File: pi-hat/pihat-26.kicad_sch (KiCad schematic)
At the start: 11 parts, among them J1 Raspberry_Pi_4, J10 Conn_01x02_Pin, J11 Conn_01x02_Pin, J12 Conn_01x02_Pin, J2 Conn_01x10_Pin, J3 Conn_01x02_Pin, J4 Conn_01x02_Pin, J5 Conn_01x02_Pin, J6 Conn_01x02_Pin, J7 Conn_01x02_Pin, J9 Conn_01x02_Pin

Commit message: Update 40 Pin Connector to KiCad template one
Also added reset button, and removed the connection to pins 27/28 which
are used for flashing the Rasperry PI config through an EEPROM, which we
don't need to do.
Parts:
- removed J1: Raspberry_Pi_4, symbol Connector:Raspberry_Pi_4
- removed J2: Conn_01x10_Pin, Package_DFN_QFN:QFN-20-1EP_5x5mm_P0.65mm_EP3.35x3.35mm, symbol Connector:Conn_01x10_Pin
- removed J9: Conn_01x02_Pin, Connector_Molex:Molex_Mini-Fit_Jr_5566-02A_2x01_P4.20mm_Vertical, symbol Connector:Conn_01x02_Pin
- added J8: GPIO, Connector_PinSocket_2.54mm:PinSocket_2x20_P2.54mm_Vertical, symbol Connector_Generic:Conn_02x20_Odd_Even
- added SW1: SW_Push, Button_Switch_THT:SW_NKK_GW12LJP, symbol Switch:SW_Push
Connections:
- net GND: now also J8.14 (Pin_14), J8.20 (Pin_20), J8.25 (Pin_25), J8.30 (Pin_30), J8.34 (Pin_34), J8.39 (Pin_39), J8.6 (Pin_6), J8.9 (Pin_9), SW1.2
- net GPIO24: now also J8.18 (Pin_18)
- net GPIO25: now also J8.22 (Pin_22)
- net GPIO26: now also J8.37 (Pin_37)
- net GPIO27: now also J8.13 (Pin_13)
- net 3_SCL_UART-RX renamed GPIO5/RXD3/SCL3
- net GPIO5/RXD3/SCL3: now also J8.29 (Pin_29)
- net 3_SDA_UART-TX renamed GPIO4/TXD3/SDA3
- net GPIO4/TXD3/SDA3: now also J8.7 (Pin_7)
- net SCL1 renamed GPIO3/SCL1
- net GPIO3/SCL1: now also J8.5 (Pin_5)
- net SCL4 renamed GPIO7/SCL4
- net GPIO7/SCL4: now also J8.26 (Pin_26)
- net SCL5 renamed GPIO11/SCL5
- net GPIO11/SCL5: now also J8.23 (Pin_23)
- net SCL6 renamed GPIO23/SCL6
- net GPIO23/SCL6: now also J8.16 (Pin_16)
- net SDA1 renamed GPIO2/SDA1
- net GPIO2/SDA1: now also J8.3 (Pin_3)
- net SDA4 renamed GPIO6/SDA4
- net GPIO6/SDA4: now also J8.31 (Pin_31)
- net SDA5 renamed GPIO10/SDA5
- net GPIO10/SDA5: now also J8.19 (Pin_19)
- net SDA6 renamed GPIO22/SDA6
- net GPIO22/SDA6: now also J8.15 (Pin_15)
- net UART0-RX renamed GPIO15/RXD0
- net GPIO15/RXD0: now also J8.10 (Pin_10)
- net UART0-TX renamed GPIO14/TXD0
- net GPIO14/TXD0: now also J8.8 (Pin_8)
- net UART4-RX renamed GPIO9/RXD4
- net GPIO9/RXD4: now also J8.21 (Pin_21)
- net UART4-TX renamed GPIO8/TXD4
- net GPIO8/TXD4: now also J8.24 (Pin_24)
- net UART5-RX renamed GPIO13/RXD5
- net GPIO13/RXD5: now also J8.33 (Pin_33)
- net UART5-TX renamed GPIO12/TXD5
- net GPIO12/TXD5: now also J8.32 (Pin_32)
- new net +3V3: J8.1 (Pin_1), J8.17 (Pin_17)
- new net +5V: J8.2 (Pin_2), J8.4 (Pin_4)
- new net GPIO16: J8.36 (Pin_36)
- new net GPIO17: J8.11 (Pin_11), SW1.1
- new net GPIO18/PCM.CLK: J8.12 (Pin_12)
- new net GPIO19/PCM.FS: J8.35 (Pin_35)
- new net GPIO20/PCM.DIN: J8.38 (Pin_38)
- new net GPIO21/PCM.DOUT: J8.40 (Pin_40)
- no-connect marks 0 -> 2
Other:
- note added: "Extended throughhole for exposing pins on the HAT. And connction to the PI"
- note added: "PIN: 27/28 is for EEPROM flashing"
- note added: "Programmable Button for Rebooting or Relaunching UI"
- note added: "Setting GPIO Alternate Functions https://www.raspberrypi.com/documentation/computers/config_txt.html#gpio-control"
- note added: "TODO: Test all UART and I2C pins, to prove they actually work, because data sheet says they do but I don't believe it Reset Button, Reboots the PI, Reboots UI? Status LEDs?"
- note removed: "GPIO 10 - SDA5 GPIO 11 - SCL5"
- note removed: "GPIO 12 - UART5_TX GPIO 13 - UART5_RX"
- note removed: "GPIO 14 - UART0-TX GPIO 15 - UART0-RX"
- note removed: "GPIO 2 - SDA1 GPIO 3 - SCL1"
- note removed: "GPIO 22 - SDA6 GPIO 23 - SCL6"
- note removed: "GPIO 8 - UART4_TX GPIO 9 - UART4_RX"
- note removed: "GPIO0 - SDA0 || UART2-TX GPIO1 - SCL0 || UART2-RX"
- note removed: "GPIO4 - SDA3 || UART3-TX GPIO5 - SCL3 || UART3-RX"
- note removed: "GPIO6 - SDA4 GPIO7 - SCL4"
- moved on the sheet: J10, J11, J12, J3, J4, J5, J6, J7

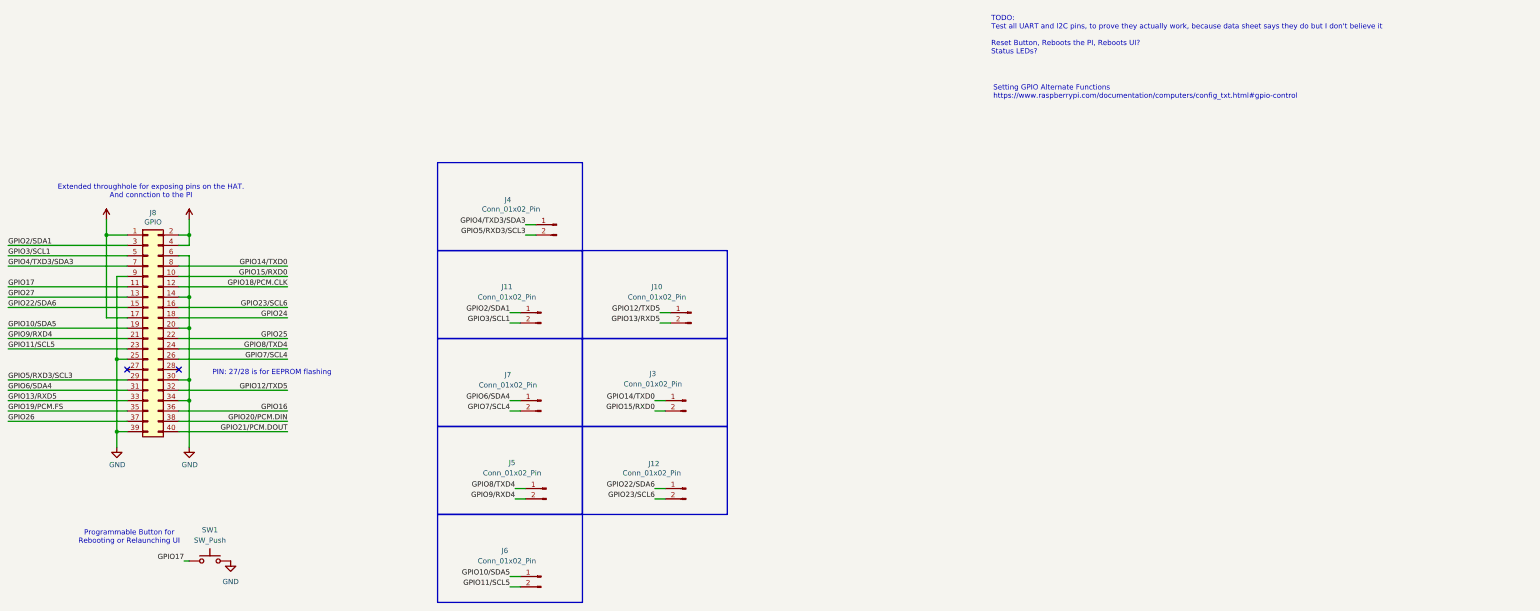
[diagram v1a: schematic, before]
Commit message: Reorganize and add 2 status LEDs to schematic
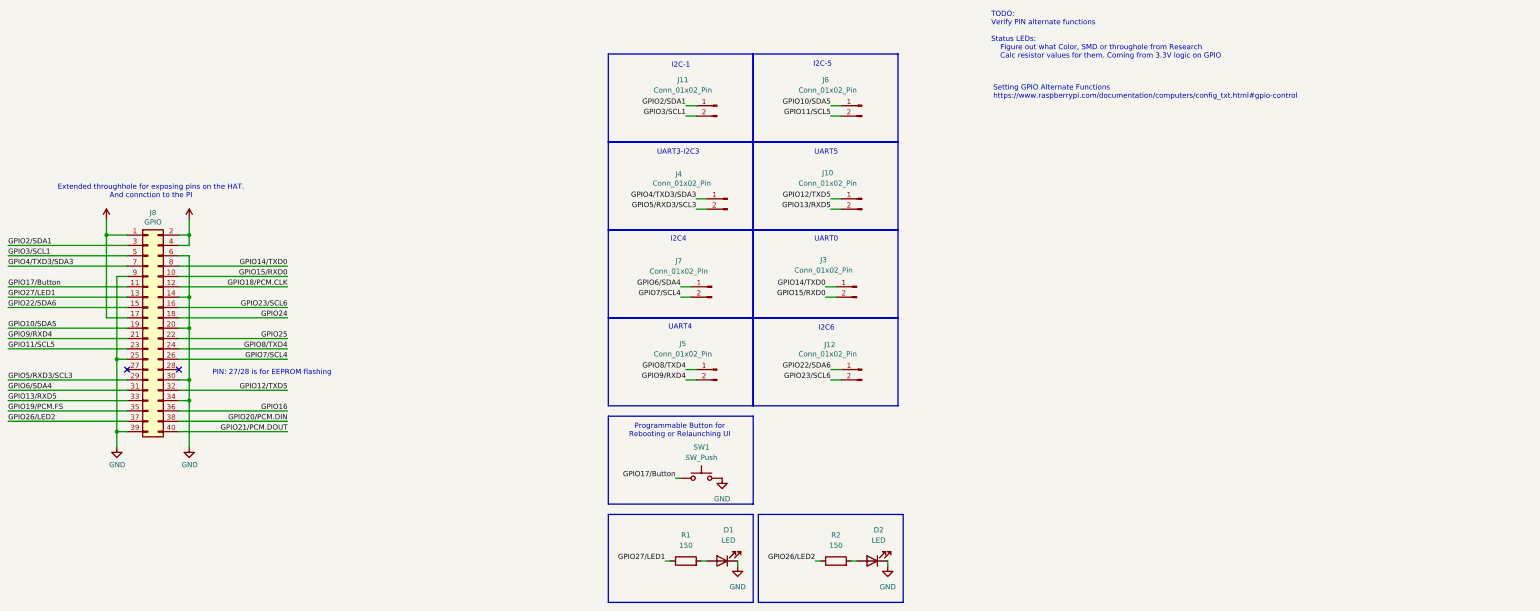
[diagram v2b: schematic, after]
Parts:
- added D1, D2: LED, symbol Device:LED
- added R1, R2: 150, symbol Device:R
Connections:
- net GND: now also D1.1 (K), D2.1 (K)
- net GPIO17 renamed GPIO17/Button
- net GPIO26 renamed GPIO26/LED2
- net GPIO26/LED2: now also R2.1
- net GPIO27 renamed GPIO27/LED1
- net GPIO27/LED1: now also R1.1
- new net: D2.2 (A), R2.2
- new net: D1.2 (A), R1.2
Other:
- note added: "I2C-1"
- note added: "I2C-5"
- note added: "I2C4"
- note added: "I2C6"
- note added: "TODO: Verify PIN alternate functions Status LEDs: Figure out what Color, SMD or throughole from Research Calc resistor values for them. Coming from 3.3V logic on GPIO"
- note added: "UART0"
- note added: "UART3-I2C3"
- note added: "UART4"
- note added: "UART5"
- note removed: "TODO: Test all UART and I2C pins, to prove they actually work, because data sheet says they do but I don't believe it Reset Button, Reboots the PI, Reboots UI? Status LEDs?"
- moved on the sheet: J10, J11, J12, J3, J4, J5, J6, J7, SW1

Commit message: Add Green,Red LED resistor values
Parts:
- R2: value 150 -> 120
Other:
- note added: "(3.3-2.2)/10mA = ~120"
- note added: "(3.3-2V)/10mA = ~150"
- note added: "GREEN-LED, 2.2V"
- note added: "RED-LED, 2V"
- note added: "TODO: Get actual LED specs if these aren't good enough"
- note added: "TODO: Verify PIN alternate functions"
- note removed: "TODO: Verify PIN alternate functions Status LEDs: Figure out what Color, SMD or throughole from Research Calc resistor values for them. Coming from 3.3V logic on GPIO"
- moved on the sheet: D1, D2, J10, J11, J12, J3, J4, J5, J6, J7, J8, R1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

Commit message: Add footprints to LED and Resistors
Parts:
- D1, D2: footprint (none) -> LED_SMD:LED_0805_2012Metric_Pad1.15x1.40mm_HandSolder
- R1, R2: footprint (none) -> Resistor_SMD:R_1206_3216Metric_Pad1.30x1.75mm_HandSolder
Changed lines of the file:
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@@
 			)
 		)
-		(property "Footprint" ""
+		(property "Footprint" "Resistor_SMD:R_1206_3216Metric_Pad1.30x1.75mm_HandSolder"
 			(at 106.68 164.338 90)
 			(hide yes)
@@
 			)
 		)
-		(property "Footprint" ""
+		(property "Footprint" "LED_SMD:LED_0805_2012Metric_Pad1.15x1.40mm_HandSolder"
 			(at 80.01 162.56 0)
 			(hide yes)
@@
 			)
 		)
-		(property "Footprint" ""
+		(property "Footprint" "LED_SMD:LED_0805_2012Metric_Pad1.15x1.40mm_HandSolder"
 			(at 115.57 162.56 0)
 			(hide yes)
@@
 			)
 		)
-		(property "Footprint" ""
+		(property "Footprint" "Resistor_SMD:R_1206_3216Metric_Pad1.30x1.75mm_HandSolder"
 			(at 71.12 164.338 90)
 			(hide yes)

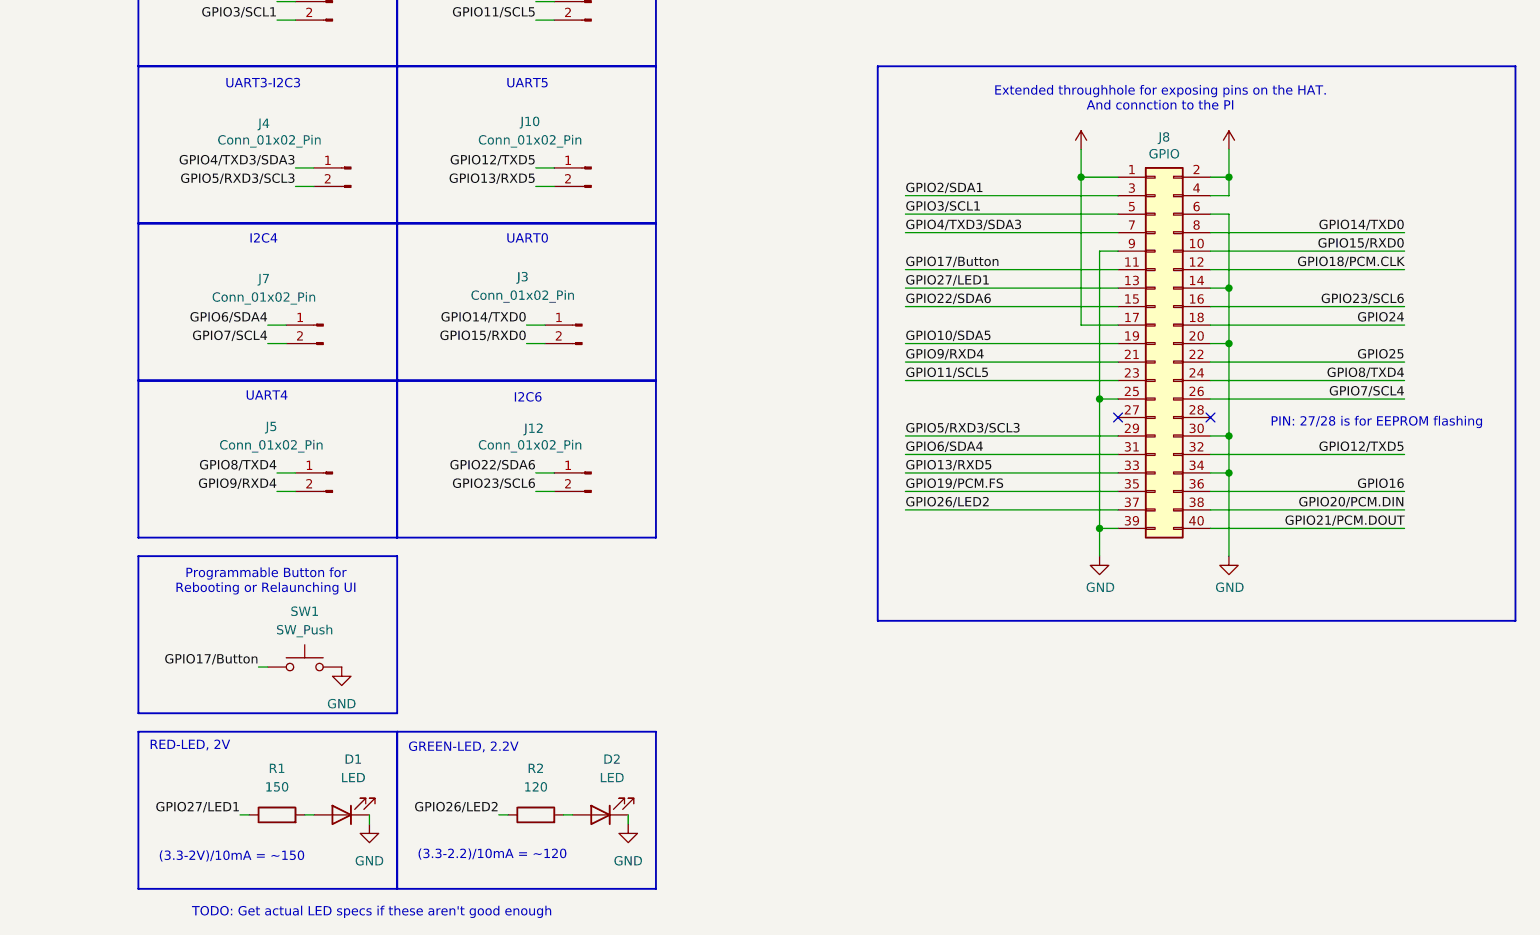
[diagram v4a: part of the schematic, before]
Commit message: Fix ERC errors
my goat swizz ty
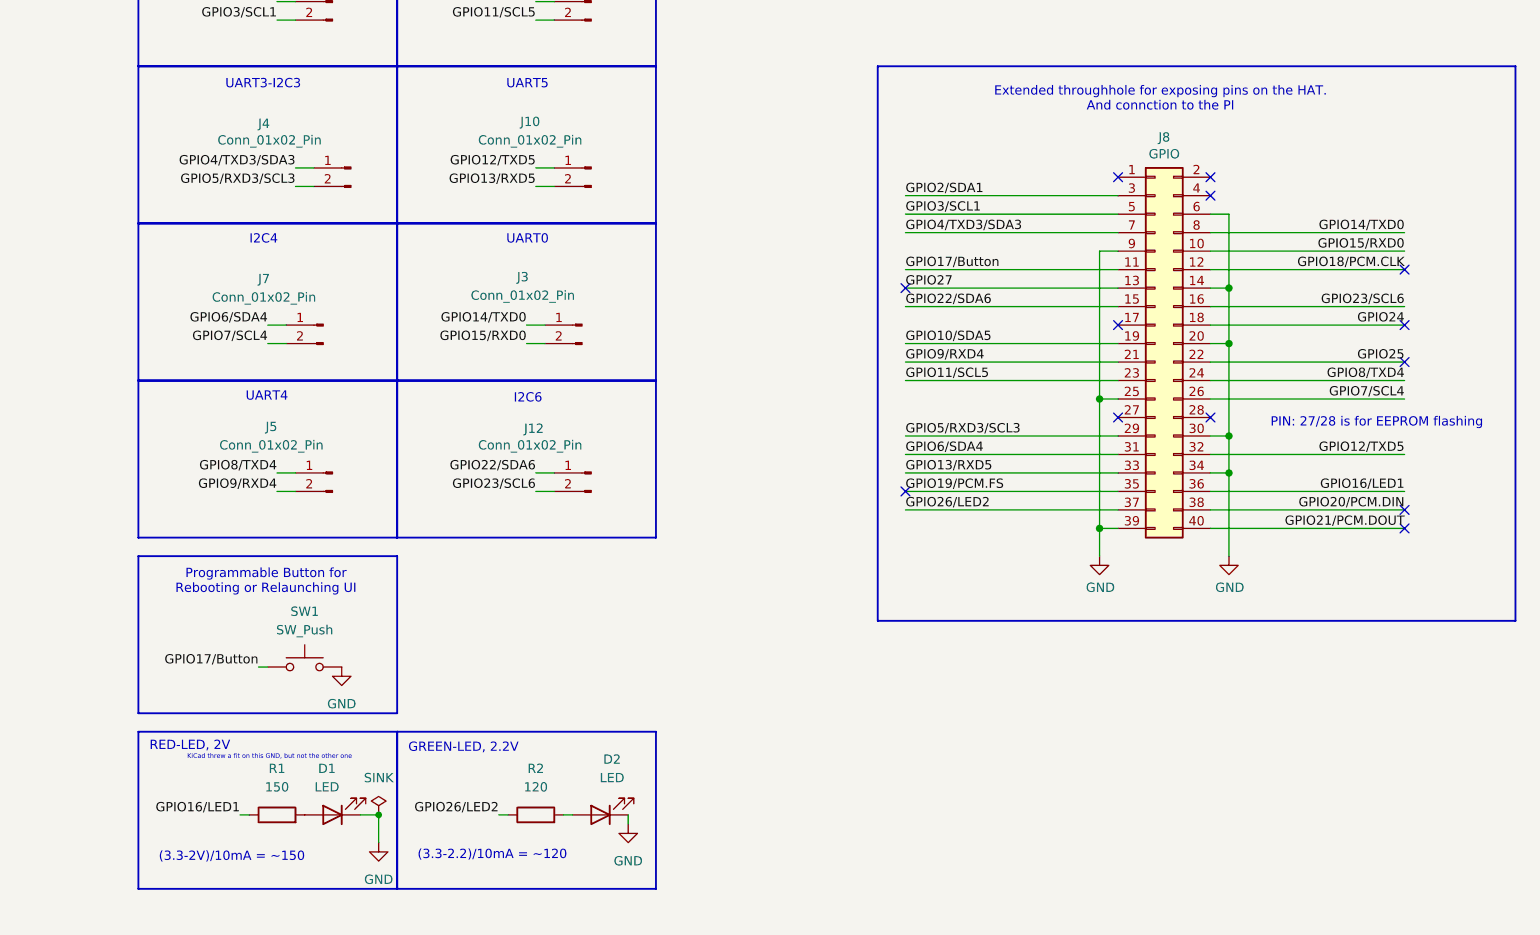
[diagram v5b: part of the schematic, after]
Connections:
- net +3V3: no longer names the net of J8.1 (Pin_1)
- net +3V3: no longer J8.17 (Pin_17)
- net +5V: no longer names the net of J8.2 (Pin_2)
- net +5V: no longer J8.4 (Pin_4)
- net GPIO16 renamed GPIO16/LED1
- net GPIO16/LED1: now also R1.1
- net GPIO27/LED1 renamed GPIO27
- net GPIO27: no longer R1.1
- no-connect marks 2 -> 13
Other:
- note added: "KiCad threw a fit on this GND, but not the other one"
- note removed: "TODO: Get actual LED specs if these aren't good enough"
- moved on the sheet: D1
